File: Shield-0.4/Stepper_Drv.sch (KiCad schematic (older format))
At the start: 92 parts, among them J16 VREF, J17 VREF, J2 VREF, J3 VREF, U1 A4982SLPTR, U2 A4982SLPTR, U5 A4982SLPTR, U7 A4982SLPTR, U9 MCP44X1

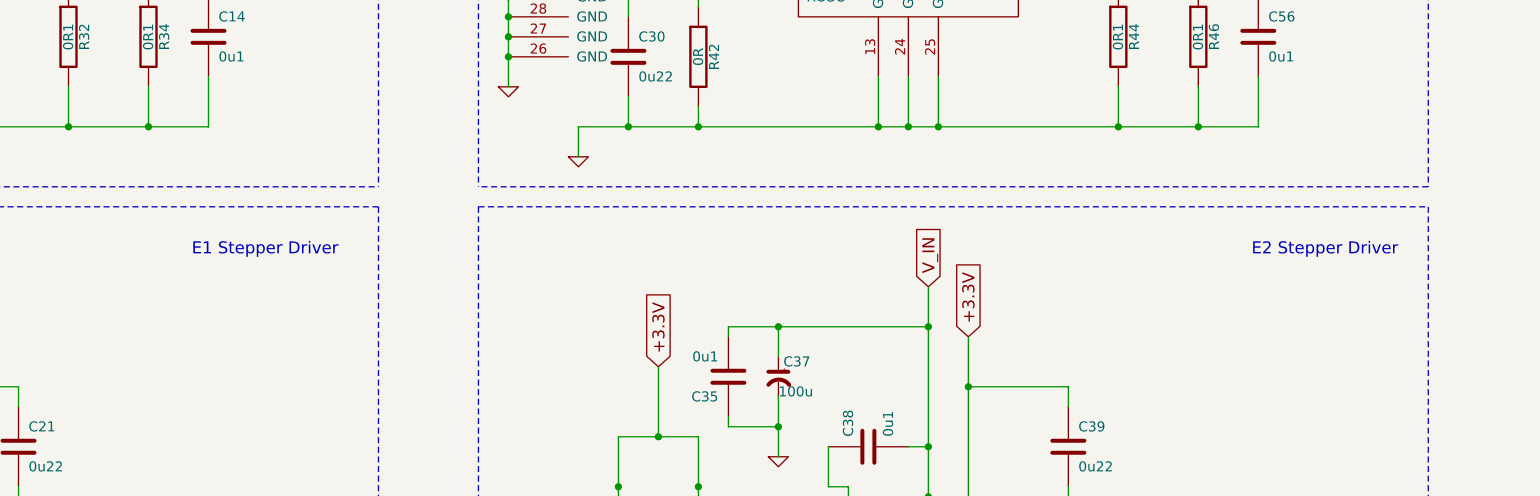
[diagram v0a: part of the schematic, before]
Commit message: Error in R26 size (it should be 0603) spotted by Wany corrected.
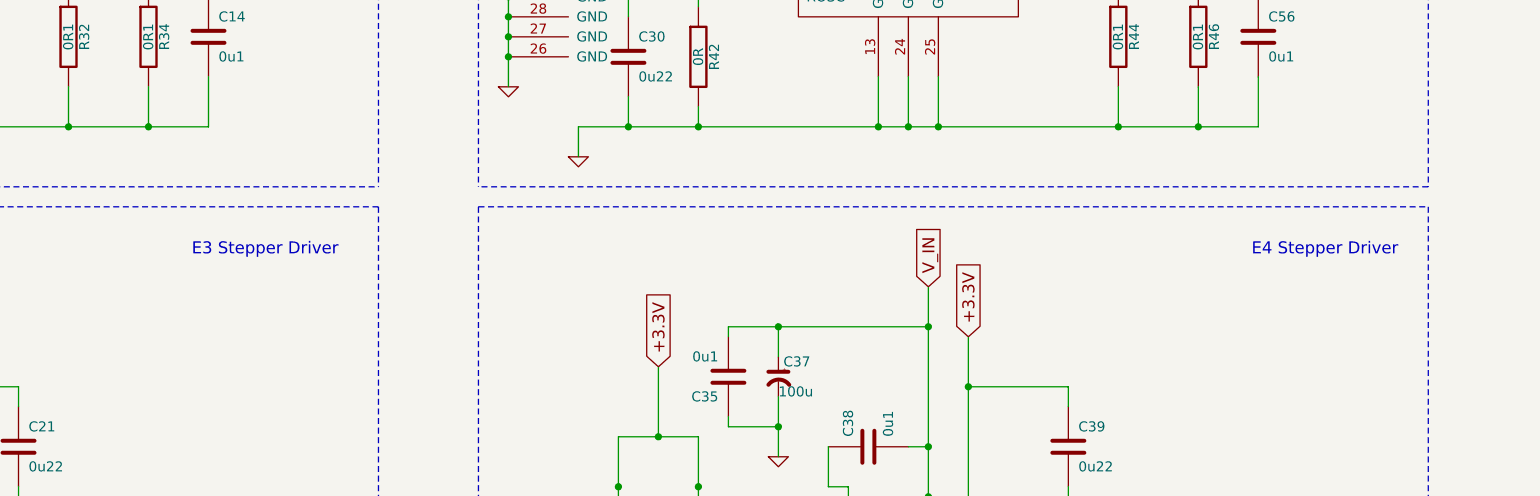
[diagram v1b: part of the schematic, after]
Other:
- note added: "E3 Stepper Driver"
- note added: "E4 Stepper Driver"
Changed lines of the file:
@@
 Sheet 2 4
 Title "Duet"
-Date "25 mar 2015"
+Date "11 jun 2015"
 Rev "0.7"
 Comp "Think3DPrint3D, RepRapPro"
@@
 $EndComp
 Text Notes 11000 6000 2    60   ~ 0
-E2 Stepper Driver
+E4 Stepper Driver
 Text Notes 5700 6000 2    60   ~ 0
-E1 Stepper Driver
+E3 Stepper Driver
 Text GLabel 10650 9050 2    60   Input ~ 0
 E4_REF
